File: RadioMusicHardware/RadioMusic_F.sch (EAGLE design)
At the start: 30 parts, among them X1 VERT_SD_CARD

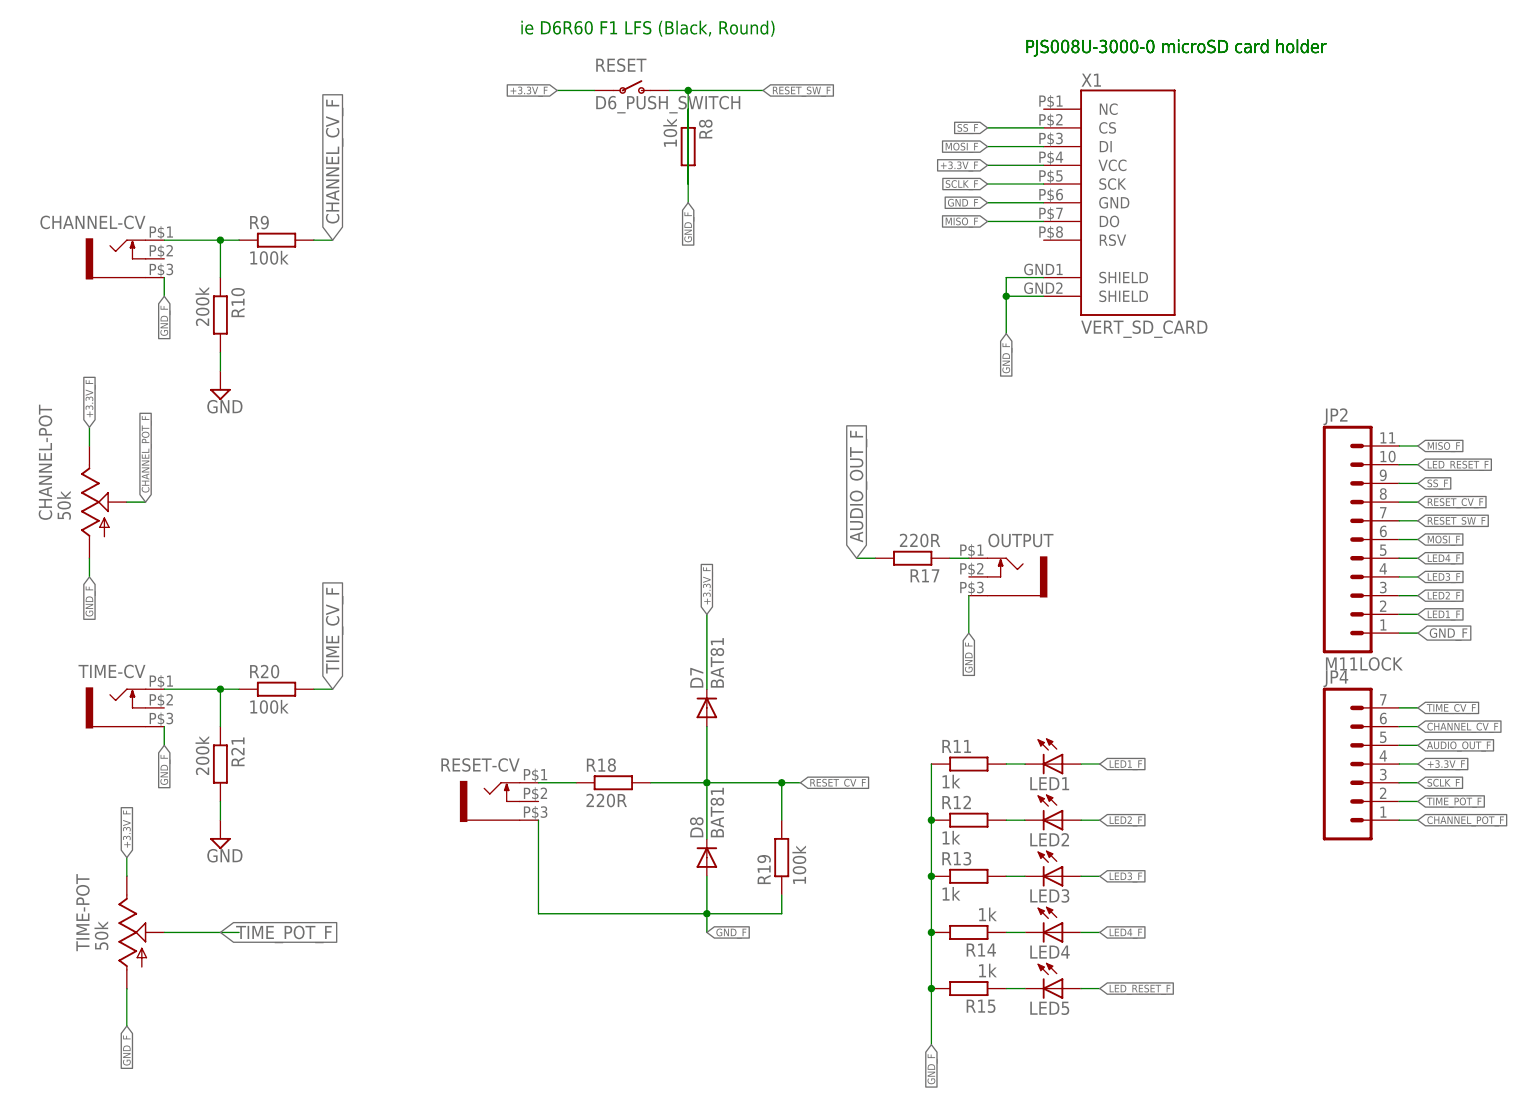
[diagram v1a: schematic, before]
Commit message: Routed boards for checking
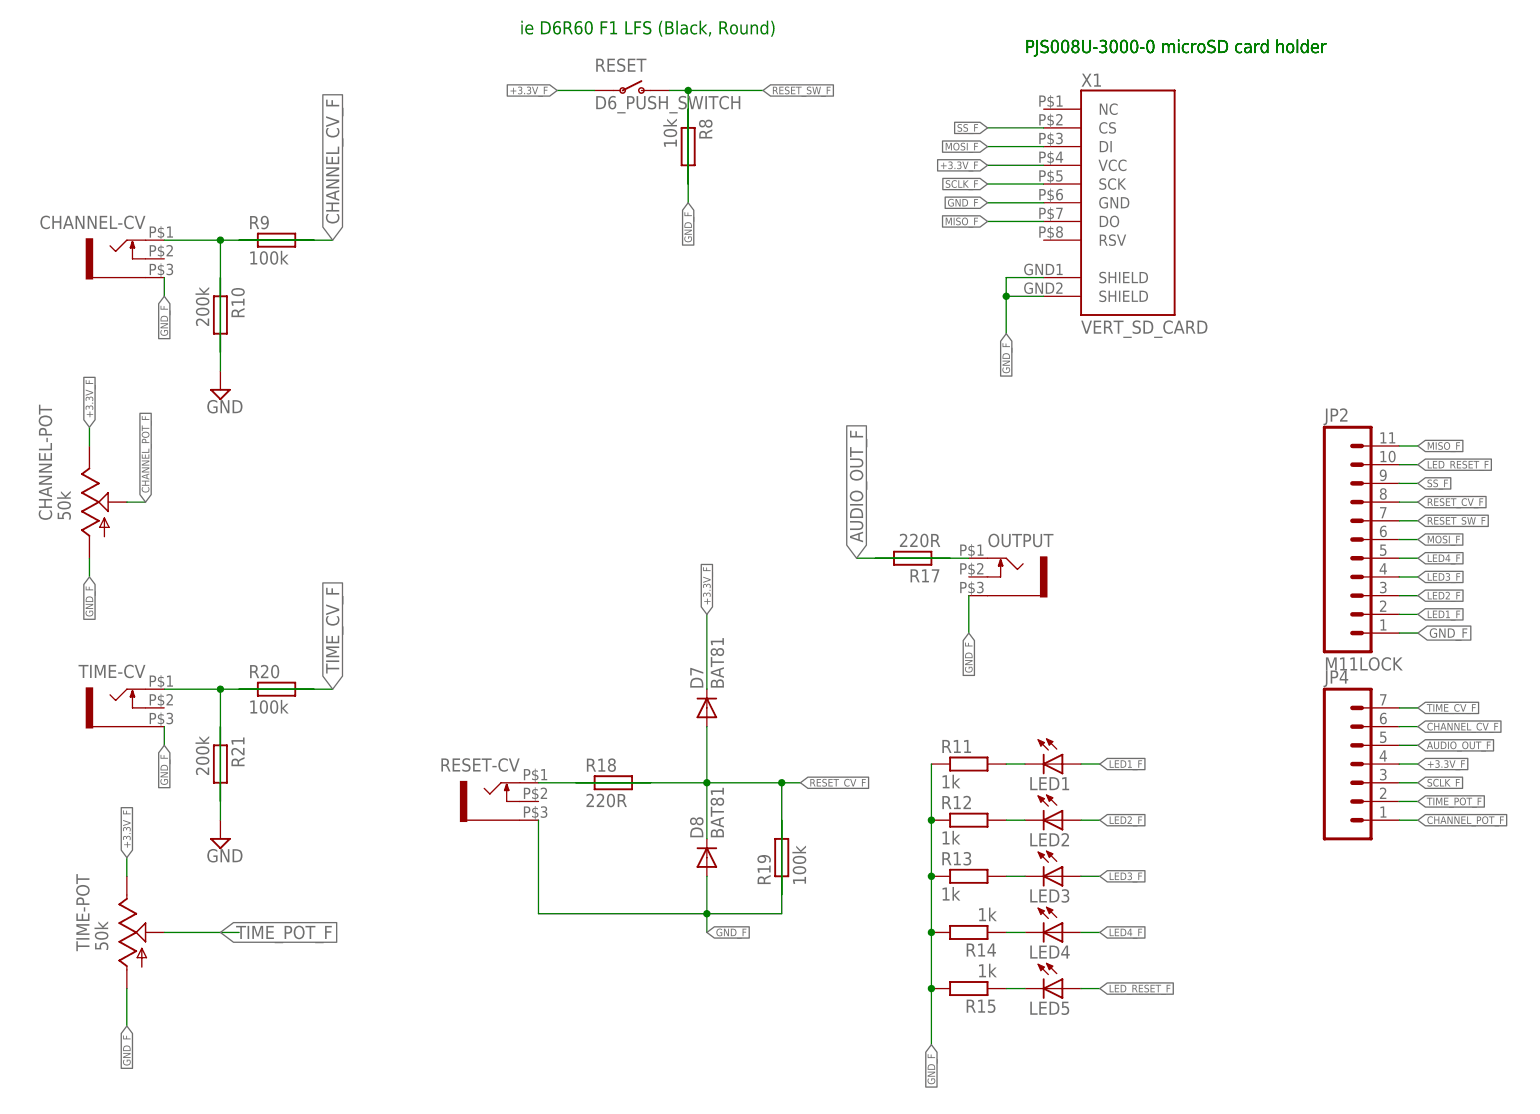
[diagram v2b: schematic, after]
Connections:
- net AUDIO_OUT_F: now also R17.1; no longer R17.2
- net CHANNEL_CV_F: now also R9.1; no longer R9.2
- net GND: now also R10.1, R21.1; no longer R10.2, R21.2
- net GND_F: now also R19.2; no longer R19.1
- net N$14: now also R18.2; no longer R18.1
- net N$3: now also R17.2; no longer R17.1
- net N$9: now also R10.2, R9.2; no longer R10.1, R9.1
- net RESET_CV_F: now also R18.1, R19.1; no longer R18.2, R19.2
- net TEMP: now also R20.2, R21.2; no longer R20.1, R21.1
- net TIME_CV_F: now also R20.1; no longer R20.2
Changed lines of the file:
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@@
 <net name="GND" class="2">
 <segment>
-<pinref part="R10" gate="G$1" pin="2"/>
-<wire x1="43.18" y1="101.6" x2="43.18" y2="99.06" width="0.1524" layer="91"/>
+<pinref part="R10" gate="G$1" pin="1"/>
+<wire x1="43.18" y1="111.76" x2="43.18" y2="99.06" width="0.1524" layer="91"/>
 <pinref part="SUPPLY4" gate="GND" pin="GND"/>
 </segment>
 <segment>
-<pinref part="R21" gate="G$1" pin="2"/>
-<wire x1="43.18" y1="40.64" x2="43.18" y2="38.1" width="0.1524" layer="91"/>
+<pinref part="R21" gate="G$1" pin="1"/>
+<wire x1="43.18" y1="50.8" x2="43.18" y2="38.1" width="0.1524" layer="91"/>
 <pinref part="SUPPLY5" gate="GND" pin="GND"/>
 </segment>
@@
 <net name="N$14" class="0">
 <segment>
-<pinref part="R18" gate="G$1" pin="1"/>
+<pinref part="R18" gate="G$1" pin="2"/>
 <pinref part="RESET-CV" gate="G$1" pin="2"/>
-<wire x1="91.44" y1="43.18" x2="86.36" y2="43.18" width="0.1524" layer="91"/>
+<wire x1="101.6" y1="43.18" x2="86.36" y2="43.18" width="0.1524" layer="91"/>
 </segment>
 </net>
@@
 </segment>
 <segment>
-<pinref part="R17" gate="G$1" pin="2"/>
-<wire x1="129.54" y1="73.66" x2="132.08" y2="73.66" width="0.1524" layer="91"/>
+<pinref part="R17" gate="G$1" pin="1"/>
+<wire x1="129.54" y1="73.66" x2="142.24" y2="73.66" width="0.1524" layer="91"/>
 <label x="129.54" y="73.66" size="1.778" layer="95" rot="R90" xref="yes"/>
 </segment>
@@
 </segment>
 </net>
-<net name="GND_F" class="0">
+<net name="GND_F" class="2">
 <segment>
 <pinref part="X1" gate="G$1" pin="GND"/>
@@
 <pinref part="RESET-CV" gate="G$1" pin="1"/>
 <wire x1="86.36" y1="38.1" x2="86.36" y2="25.4" width="0.1524" layer="91"/>
-<pinref part="R19" gate="G$1" pin="1"/>
-<wire x1="119.38" y1="27.94" x2="119.38" y2="25.4" width="0.1524" layer="91"/>
+<pinref part="R19" gate="G$1" pin="2"/>
+<wire x1="119.38" y1="38.1" x2="119.38" y2="25.4" width="0.1524" layer="91"/>
 <pinref part="D8" gate="1" pin="A"/>
 <wire x1="109.22" y1="25.4" x2="109.22" y2="30.48" width="0.1524" layer="91"/>
@@
 </segment>
 <segment>
-<pinref part="R9" gate="G$1" pin="2"/>
-<wire x1="58.42" y1="116.84" x2="55.88" y2="116.84" width="0.1524" layer="91"/>
+<pinref part="R9" gate="G$1" pin="1"/>
+<wire x1="58.42" y1="116.84" x2="45.72" y2="116.84" width="0.1524" layer="91"/>
 <label x="58.42" y="116.84" size="1.778" layer="95" rot="R90" xref="yes"/>
 </segment>
@@
 </segment>
 <segment>
-<pinref part="R20" gate="G$1" pin="2"/>
-<wire x1="58.42" y1="55.88" x2="55.88" y2="55.88" width="0.1524" layer="91"/>
+<pinref part="R20" gate="G$1" pin="1"/>
+<wire x1="58.42" y1="55.88" x2="45.72" y2="55.88" width="0.1524" layer="91"/>
 <label x="58.42" y="55.88" size="1.778" layer="95" rot="R90" xref="yes"/>
 </segment>
@@
 <pinref part="D8" gate="1" pin="C"/>
 <wire x1="109.22" y1="35.56" x2="109.22" y2="43.18" width="0.1524" layer="91"/>
-<pinref part="R18" gate="G$1" pin="2"/>
+<pinref part="R18" gate="G$1" pin="1"/>
 <wire x1="109.22" y1="43.18" x2="109.22" y2="50.8" width="0.1524" layer="91"/>
-<wire x1="101.6" y1="43.18" x2="109.22" y2="43.18" width="0.1524" layer="91"/>
+<wire x1="91.44" y1="43.18" x2="109.22" y2="43.18" width="0.1524" layer="91"/>
 <junction x="109.22" y="43.18"/>
 <wire x1="109.22" y1="43.18" x2="119.38" y2="43.18" width="0.1524" layer="91"/>
-<pinref part="R19" gate="G$1" pin="2"/>
+<pinref part="R19" gate="G$1" pin="1"/>
 <wire x1="119.38" y1="43.18" x2="121.92" y2="43.18" width="0.1524" layer="91"/>
-<wire x1="119.38" y1="38.1" x2="119.38" y2="43.18" width="0.1524" layer="91"/>
+<wire x1="119.38" y1="27.94" x2="119.38" y2="43.18" width="0.1524" layer="91"/>
 <junction x="119.38" y="43.18"/>
 <label x="121.92" y="43.18" size="1.016" layer="95" xref="yes"/>
@@
 <net name="TEMP" class="0">
 <segment>
-<pinref part="R20" gate="G$1" pin="1"/>
-<wire x1="45.72" y1="55.88" x2="43.18" y2="55.88" width="0.1524" layer="91"/>
-<pinref part="R21" gate="G$1" pin="1"/>
+<pinref part="R20" gate="G$1" pin="2"/>
+<wire x1="55.88" y1="55.88" x2="43.18" y2="55.88" width="0.1524" layer="91"/>
+<pinref part="R21" gate="G$1" pin="2"/>
 <wire x1="43.18" y1="55.88" x2="35.56" y2="55.88" width="0.1524" layer="91"/>
-<wire x1="43.18" y1="50.8" x2="43.18" y2="55.88" width="0.1524" layer="91"/>
+<wire x1="43.18" y1="40.64" x2="43.18" y2="55.88" width="0.1524" layer="91"/>
 <junction x="43.18" y="55.88"/>
 <pinref part="TIME-CV" gate="G$1" pin="2"/>
@@
 <net name="N$9" class="0">
 <segment>
-<pinref part="R9" gate="G$1" pin="1"/>
+<pinref part="R9" gate="G$1" pin="2"/>
 <pinref part="CHANNEL-CV" gate="G$1" pin="2"/>
-<wire x1="45.72" y1="116.84" x2="43.18" y2="116.84" width="0.1524" layer="91"/>
-<pinref part="R10" gate="G$1" pin="1"/>
+<wire x1="55.88" y1="116.84" x2="43.18" y2="116.84" width="0.1524" layer="91"/>
+<pinref part="R10" gate="G$1" pin="2"/>
 <wire x1="43.18" y1="116.84" x2="35.56" y2="116.84" width="0.1524" layer="91"/>
-<wire x1="43.18" y1="111.76" x2="43.18" y2="116.84" width="0.1524" layer="91"/>
+<wire x1="43.18" y1="101.6" x2="43.18" y2="116.84" width="0.1524" layer="91"/>
 <junction x="43.18" y="116.84"/>
 </segment>
@@
 <segment>
 <pinref part="OUTPUT" gate="G$1" pin="2"/>
-<pinref part="R17" gate="G$1" pin="1"/>
-<wire x1="142.24" y1="73.66" x2="144.78" y2="73.66" width="0.1524" layer="91"/>
-</segment>
-</net>
+<pinref part="R17" gate="G$1" pin="2"/>
+<wire x1="132.08" y1="73.66" x2="144.78" y2="73.66" width="0.1524" layer="91"/>
+</segment>
+</net>

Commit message: PCB cosmetic changes
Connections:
- net +3.3V_F: now also X1.VCC/+; no longer X1.VCC
- net MISO_F: now also X1.DO/MISO; no longer X1.DO
- net MOSI_F: now also X1.DI/MOSI; no longer X1.DI
- net SCLK_F: now also X1.CLK/SCK; no longer X1.SCK
- net SS_F: now also X1.CS/SS; no longer X1.CS
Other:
- moved on the sheet: R10, R17, R18, R20, R21, R8, R9
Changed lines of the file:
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@@
 <instance part="RESET-CV" gate="G$1" x="81.28" y="40.64" rot="MR0"/>
 <instance part="OUTPUT" gate="G$1" x="149.86" y="71.12"/>
-<instance part="R9" gate="G$1" x="50.8" y="116.84"/>
-<instance part="R10" gate="G$1" x="43.18" y="106.68" rot="R270"/>
+<instance part="R9" gate="G$1" x="50.8" y="116.84" rot="R180"/>
+<instance part="R10" gate="G$1" x="43.18" y="106.68" rot="R90"/>
 <instance part="SUPPLY4" gate="GND" x="43.18" y="96.52"/>
-<instance part="R17" gate="G$1" x="137.16" y="73.66" rot="R180"/>
+<instance part="R17" gate="G$1" x="137.16" y="73.66"/>
 <instance part="TIME-POT" gate="G$1" x="30.48" y="22.86"/>
 <instance part="TIME-CV" gate="G$1" x="30.48" y="53.34" rot="MR0"/>
-<instance part="R20" gate="G$1" x="50.8" y="55.88"/>
-<instance part="R21" gate="G$1" x="43.18" y="45.72" rot="R270"/>
+<instance part="R20" gate="G$1" x="50.8" y="55.88" rot="R180"/>
+<instance part="R21" gate="G$1" x="43.18" y="45.72" rot="R90"/>
 <instance part="SUPPLY5" gate="GND" x="43.18" y="35.56"/>
 <instance part="D7" gate="1" x="109.22" y="53.34" rot="R90"/>
 <instance part="D8" gate="1" x="109.22" y="33.02" rot="R90"/>
 <instance part="R19" gate="G$1" x="119.38" y="33.02" rot="R90"/>
-<instance part="R18" gate="G$1" x="96.52" y="43.18"/>
+<instance part="R18" gate="G$1" x="96.52" y="43.18" rot="R180"/>
 <instance part="RESET" gate="G$1" x="99.06" y="137.16"/>
-<instance part="R8" gate="G$1" x="106.68" y="129.54" rot="R270"/>
+<instance part="R8" gate="G$1" x="106.68" y="129.54" rot="R90"/>
 <instance part="LED1" gate="G$1" x="157.48" y="45.72" rot="R270"/>
 <instance part="LED2" gate="G$1" x="157.48" y="38.1" rot="R270"/>
@@
 <segment>
 <pinref part="R10" gate="G$1" pin="1"/>
-<wire x1="43.18" y1="111.76" x2="43.18" y2="99.06" width="0.1524" layer="91"/>
+<wire x1="43.18" y1="101.6" x2="43.18" y2="99.06" width="0.1524" layer="91"/>
 <pinref part="SUPPLY4" gate="GND" pin="GND"/>
 </segment>
 <segment>
 <pinref part="R21" gate="G$1" pin="1"/>
-<wire x1="43.18" y1="50.8" x2="43.18" y2="38.1" width="0.1524" layer="91"/>
+<wire x1="43.18" y1="40.64" x2="43.18" y2="38.1" width="0.1524" layer="91"/>
 <pinref part="SUPPLY5" gate="GND" pin="GND"/>
 </segment>
@@
 <pinref part="R18" gate="G$1" pin="2"/>
 <pinref part="RESET-CV" gate="G$1" pin="2"/>
-<wire x1="101.6" y1="43.18" x2="86.36" y2="43.18" width="0.1524" layer="91"/>
+<wire x1="91.44" y1="43.18" x2="86.36" y2="43.18" width="0.1524" layer="91"/>
 </segment>
 </net>
@@
 <net name="MISO_F" class="0">
 <segment>
-<pinref part="X1" gate="G$1" pin="DO"/>
+<pinref part="X1" gate="G$1" pin="DO/MISO"/>
 <wire x1="147.32" y1="119.38" x2="154.94" y2="119.38" width="0.1524" layer="91"/>
 <label x="147.32" y="119.38" size="1.016" layer="95" rot="R180" xref="yes"/>
@@
 <segment>
 <pinref part="R17" gate="G$1" pin="1"/>
-<wire x1="129.54" y1="73.66" x2="142.24" y2="73.66" width="0.1524" layer="91"/>
+<wire x1="129.54" y1="73.66" x2="132.08" y2="73.66" width="0.1524" layer="91"/>
 <label x="129.54" y="73.66" size="1.778" layer="95" rot="R90" xref="yes"/>
 </segment>
@@
 <pinref part="R8" gate="G$1" pin="2"/>
 <wire x1="106.68" y1="137.16" x2="116.84" y2="137.16" width="0.1524" layer="91"/>
-<wire x1="106.68" y1="124.46" x2="106.68" y2="137.16" width="0.1524" layer="91"/>
+<wire x1="106.68" y1="134.62" x2="106.68" y2="137.16" width="0.1524" layer="91"/>
 <junction x="106.68" y="137.16"/>
 <label x="116.84" y="137.16" size="1.016" layer="95" xref="yes"/>
@@
 <net name="+3.3V_F" class="0">
 <segment>
-<pinref part="X1" gate="G$1" pin="VCC"/>
+<pinref part="X1" gate="G$1" pin="VCC/+"/>
 <wire x1="147.32" y1="127" x2="154.94" y2="127" width="0.1524" layer="91"/>
 <label x="147.32" y="127" size="1.016" layer="95" rot="R180" xref="yes"/>
@@
 <segment>
 <pinref part="R8" gate="G$1" pin="1"/>
-<wire x1="106.68" y1="121.92" x2="106.68" y2="134.62" width="0.1524" layer="91"/>
+<wire x1="106.68" y1="121.92" x2="106.68" y2="124.46" width="0.1524" layer="91"/>
 <label x="106.68" y="121.92" size="1.016" layer="95" rot="R270" xref="yes"/>
 </segment>
@@
 <segment>
 <pinref part="R9" gate="G$1" pin="1"/>
-<wire x1="58.42" y1="116.84" x2="45.72" y2="116.84" width="0.1524" layer="91"/>
+<wire x1="58.42" y1="116.84" x2="55.88" y2="116.84" width="0.1524" layer="91"/>
 <label x="58.42" y="116.84" size="1.778" layer="95" rot="R90" xref="yes"/>
 </segment>
@@
 <segment>
 <pinref part="R20" gate="G$1" pin="1"/>
-<wire x1="58.42" y1="55.88" x2="45.72" y2="55.88" width="0.1524" layer="91"/>
+<wire x1="58.42" y1="55.88" x2="55.88" y2="55.88" width="0.1524" layer="91"/>
 <label x="58.42" y="55.88" size="1.778" layer="95" rot="R90" xref="yes"/>
 </segment>
@@
 <pinref part="R18" gate="G$1" pin="1"/>
 <wire x1="109.22" y1="43.18" x2="109.22" y2="50.8" width="0.1524" layer="91"/>
-<wire x1="91.44" y1="43.18" x2="109.22" y2="43.18" width="0.1524" layer="91"/>
+<wire x1="101.6" y1="43.18" x2="109.22" y2="43.18" width="0.1524" layer="91"/>
 <junction x="109.22" y="43.18"/>
 <wire x1="109.22" y1="43.18" x2="119.38" y2="43.18" width="0.1524" layer="91"/>
@@
 <net name="SCLK_F" class="0">
 <segment>
-<pinref part="X1" gate="G$1" pin="SCK"/>
+<pinref part="X1" gate="G$1" pin="CLK/SCK"/>
 <wire x1="147.32" y1="124.46" x2="154.94" y2="124.46" width="0.1524" layer="91"/>
 <label x="147.32" y="124.46" size="1.016" layer="95" rot="R180" xref="yes"/>
@@
 <net name="MOSI_F" class="0">
 <segment>
-<pinref part="X1" gate="G$1" pin="DI"/>
+<pinref part="X1" gate="G$1" pin="DI/MOSI"/>
 <wire x1="147.32" y1="129.54" x2="154.94" y2="129.54" width="0.1524" layer="91"/>
 <label x="147.32" y="129.54" size="1.016" layer="95" rot="R180" xref="yes"/>
@@
 <net name="SS_F" class="0">
 <segment>
-<pinref part="X1" gate="G$1" pin="CS"/>
+<pinref part="X1" gate="G$1" pin="CS/SS"/>
 <wire x1="147.32" y1="132.08" x2="154.94" y2="132.08" width="0.1524" layer="91"/>
 <label x="147.32" y="132.08" size="1.016" layer="95" rot="R180" xref="yes"/>
@@
 <segment>
 <pinref part="R20" gate="G$1" pin="2"/>
-<wire x1="55.88" y1="55.88" x2="43.18" y2="55.88" width="0.1524" layer="91"/>
+<wire x1="45.72" y1="55.88" x2="43.18" y2="55.88" width="0.1524" layer="91"/>
 <pinref part="R21" gate="G$1" pin="2"/>
 <wire x1="43.18" y1="55.88" x2="35.56" y2="55.88" width="0.1524" layer="91"/>
-<wire x1="43.18" y1="40.64" x2="43.18" y2="55.88" width="0.1524" layer="91"/>
+<wire x1="43.18" y1="50.8" x2="43.18" y2="55.88" width="0.1524" layer="91"/>
 <junction x="43.18" y="55.88"/>
 <pinref part="TIME-CV" gate="G$1" pin="2"/>
@@
 <pinref part="R9" gate="G$1" pin="2"/>
 <pinref part="CHANNEL-CV" gate="G$1" pin="2"/>
-<wire x1="55.88" y1="116.84" x2="43.18" y2="116.84" width="0.1524" layer="91"/>
+<wire x1="45.72" y1="116.84" x2="43.18" y2="116.84" width="0.1524" layer="91"/>
 <pinref part="R10" gate="G$1" pin="2"/>
 <wire x1="43.18" y1="116.84" x2="35.56" y2="116.84" width="0.1524" layer="91"/>
-<wire x1="43.18" y1="101.6" x2="43.18" y2="116.84" width="0.1524" layer="91"/>
+<wire x1="43.18" y1="111.76" x2="43.18" y2="116.84" width="0.1524" layer="91"/>
 <junction x="43.18" y="116.84"/>
 </segment>
@@
 <pinref part="OUTPUT" gate="G$1" pin="2"/>
 <pinref part="R17" gate="G$1" pin="2"/>
-<wire x1="132.08" y1="73.66" x2="144.78" y2="73.66" width="0.1524" layer="91"/>
-</segment>
-</net>
+<wire x1="142.24" y1="73.66" x2="144.78" y2="73.66" width="0.1524" layer="91"/>
+</segment>
+</net>

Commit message: Text subbing
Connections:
- net GND_F: now also R14.1; no longer R14.2
- net N$21: now also R14.2; no longer R14.1
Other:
- moved on the sheet: R19
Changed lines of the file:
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@@
 <instance part="D7" gate="1" x="109.22" y="53.34" rot="R90"/>
 <instance part="D8" gate="1" x="109.22" y="33.02" rot="R90"/>
-<instance part="R19" gate="G$1" x="119.38" y="33.02" rot="R90"/>
+<instance part="R19" gate="G$1" x="119.38" y="33.02" rot="R270"/>
 <instance part="R18" gate="G$1" x="96.52" y="43.18" rot="R180"/>
 <instance part="RESET" gate="G$1" x="99.06" y="137.16"/>
@@
 <segment>
 <pinref part="LED4" gate="G$1" pin="C"/>
-<pinref part="R14" gate="G$1" pin="1"/>
-<wire x1="149.86" y1="22.86" x2="152.4" y2="22.86" width="0.1524" layer="91"/>
+<pinref part="R14" gate="G$1" pin="2"/>
+<wire x1="139.7" y1="22.86" x2="152.4" y2="22.86" width="0.1524" layer="91"/>
 </segment>
 </net>
@@
 <wire x1="86.36" y1="38.1" x2="86.36" y2="25.4" width="0.1524" layer="91"/>
 <pinref part="R19" gate="G$1" pin="2"/>
-<wire x1="119.38" y1="38.1" x2="119.38" y2="25.4" width="0.1524" layer="91"/>
+<wire x1="119.38" y1="27.94" x2="119.38" y2="25.4" width="0.1524" layer="91"/>
 <pinref part="D8" gate="1" pin="A"/>
 <wire x1="109.22" y1="25.4" x2="109.22" y2="30.48" width="0.1524" layer="91"/>
@@
 <junction x="139.7" y="38.1"/>
 <pinref part="R13" gate="G$1" pin="1"/>
-<wire x1="139.7" y1="30.48" x2="139.7" y2="22.86" width="0.1524" layer="91"/>
+<wire x1="139.7" y1="30.48" x2="149.86" y2="22.86" width="0.1524" layer="91"/>
 <junction x="139.7" y="30.48"/>
-<pinref part="R14" gate="G$1" pin="2"/>
-<wire x1="139.7" y1="22.86" x2="139.7" y2="15.24" width="0.1524" layer="91"/>
-<junction x="139.7" y="22.86"/>
+<pinref part="R14" gate="G$1" pin="1"/>
+<wire x1="149.86" y1="22.86" x2="139.7" y2="15.24" width="0.1524" layer="91"/>
+<junction x="149.86" y="22.86"/>
 <pinref part="R15" gate="G$1" pin="2"/>
 <wire x1="139.7" y1="15.24" x2="139.7" y2="7.62" width="0.1524" layer="91"/>
@@
 <pinref part="R19" gate="G$1" pin="1"/>
 <wire x1="119.38" y1="43.18" x2="121.92" y2="43.18" width="0.1524" layer="91"/>
-<wire x1="119.38" y1="27.94" x2="119.38" y2="43.18" width="0.1524" layer="91"/>
+<wire x1="119.38" y1="38.1" x2="119.38" y2="43.18" width="0.1524" layer="91"/>
 <junction x="119.38" y="43.18"/>
 <label x="121.92" y="43.18" size="1.016" layer="95" xref="yes"/>
